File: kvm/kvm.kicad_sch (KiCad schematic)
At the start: 61 parts, among them J1 USB4110-GF-A, J2 USB4110-GF-A, J3 USB_A_Stacked, J4 USB_A_Stacked, Q1 Q_PMOS_GSD, SW1 SW_DPDT_x2, U1 SRV05-4, U2 LTC4412xS6, U3 FSUSB42MUX, U4 GL850G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

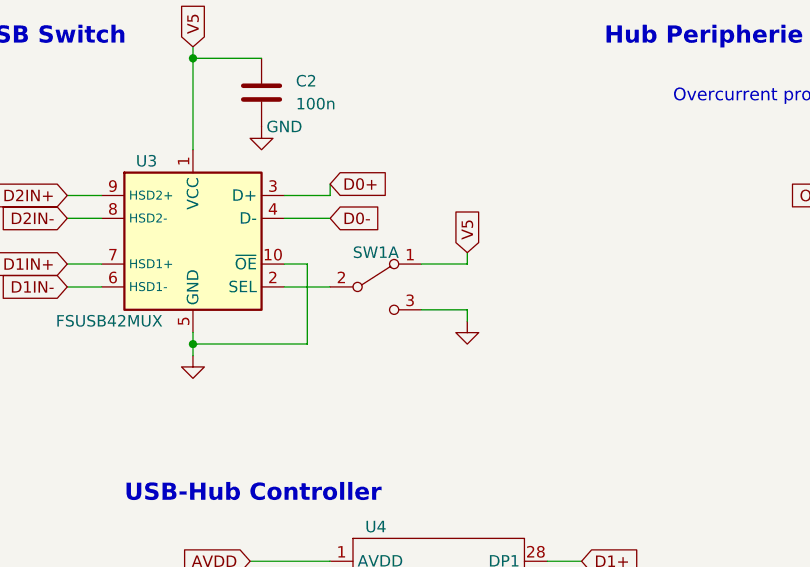
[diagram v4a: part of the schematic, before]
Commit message: fixed missing pull down on FSUSBMUX
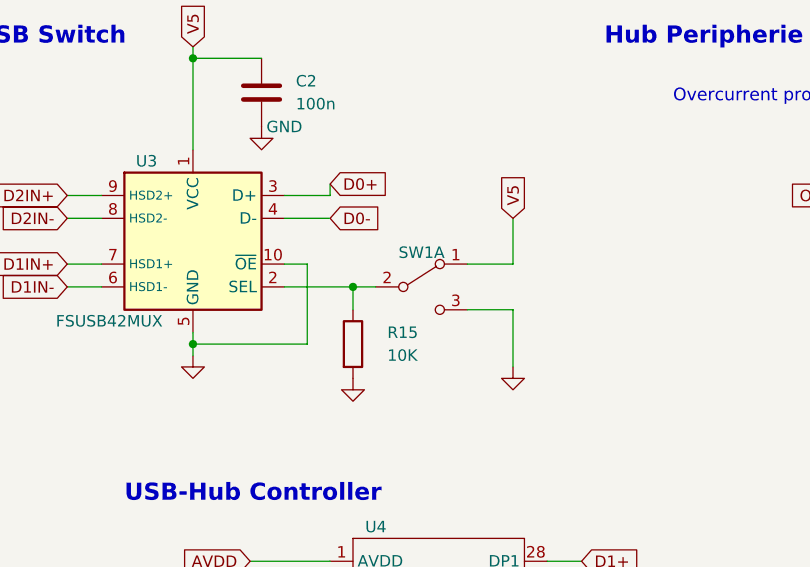
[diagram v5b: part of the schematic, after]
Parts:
- added R15: 10K, Resistor_SMD:R_0603_1608Metric_Pad0.98x0.95mm_HandSolder, symbol Device:R
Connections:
- net GND: now also R15.2
- net at SW1.2 (B), U3.2 (SEL): now also R15.1
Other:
- moved on the sheet: SW1A
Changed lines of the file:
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@@
   (junction (at 66.04 133.35) (diameter 0) (color 0 0 0 0)
   )
+  (junction (at 128.27 44.45) (diameter 0) (color 0 0 0 0)
+  )
   (junction (at 237.49 106.68) (diameter 0) (color 0 0 0 0)
   )
@@
     (stroke (width 0) (type default) (color 0 0 0 0))
   )
+  (wire (pts (xy 128.27 44.45) (xy 128.27 46.99))
+    (stroke (width 0) (type default) (color 0 0 0 0))
+  )
   (wire (pts (xy 273.05 124.46) (xy 270.51 124.46))
     (stroke (width 0) (type default) (color 0 0 0 0))
@@
     (stroke (width 0) (type default) (color 0 0 0 0))
   )
+  (wire (pts (xy 128.27 44.45) (xy 130.81 44.45))
+    (stroke (width 0) (type default) (color 0 0 0 0))
+  )
   (wire (pts (xy 29.21 158.75) (xy 33.02 158.75))
     (stroke (width 0) (type default) (color 0 0 0 0))
@@
     (stroke (width 0) (type default) (color 0 0 0 0))
   )
-  (wire (pts (xy 135.89 41.91) (xy 140.97 41.91))
+  (wire (pts (xy 140.97 41.91) (xy 146.05 41.91))
     (stroke (width 0) (type default) (color 0 0 0 0))
   )
@@
     (stroke (width 0) (type default) (color 0 0 0 0))
   )
-  (wire (pts (xy 135.89 46.99) (xy 140.97 46.99))
+  (wire (pts (xy 140.97 46.99) (xy 146.05 46.99))
     (stroke (width 0) (type default) (color 0 0 0 0))
   )
@@
     (stroke (width 0) (type default) (color 0 0 0 0))
   )
-  (wire (pts (xy 140.97 46.99) (xy 140.97 48.26))
+  (wire (pts (xy 146.05 46.99) (xy 146.05 53.34))
     (stroke (width 0) (type default) (color 0 0 0 0))
   )
@@
     (stroke (width 0) (type default) (color 0 0 0 0))
   )
-  (wire (pts (xy 140.97 40.64) (xy 140.97 41.91))
+  (wire (pts (xy 146.05 36.83) (xy 146.05 41.91))
     (stroke (width 0) (type default) (color 0 0 0 0))
   )
@@
     (stroke (width 0) (type default) (color 0 0 0 0))
   )
-  (wire (pts (xy 120.65 44.45) (xy 125.73 44.45))
+  (wire (pts (xy 120.65 44.45) (xy 128.27 44.45))
     (stroke (width 0) (type default) (color 0 0 0 0))
   )
@@
     )
   )
-  (global_label "V5" (shape input) (at 140.97 40.64 90) (fields_autoplaced)
+  (global_label "V5" (shape input) (at 146.05 36.83 90) (fields_autoplaced)
     (effects (font (size 1.27 1.27)) (justify left))
-    (property "Intersheet References" "${INTERSHEET_REFS}" (id 0) (at 140.8906 35.9288 90)
+    (property "Intersheet References" "${INTERSHEET_REFS}" (id 0) (at 145.9706 32.1188 90)
       (effects (font (size 1.27 1.27)) (justify left) hide)
     )
@@
     (pin "2")
   )
+  (symbol (lib_id "power:GND") (at 128.27 54.61 0) (unit 1)
+    (in_bom yes) (on_board yes) (fields_autoplaced)
+    (property "Reference" "#PWR04" (id 0) (at 128.27 60.96 0)
+      (effects (font (size 1.27 1.27)) hide)
+    )
+    (property "Value" "GND" (id 1) (at 128.27 59.69 0)
+      (effects (font (size 1.27 1.27)) hide)
+    )
+    (property "Footprint" "" (id 2) (at 128.27 54.61 0)
+      (effects (font (size 1.27 1.27)) hide)
+    )
+    (property "Datasheet" "" (id 3) (at 128.27 54.61 0)
+      (effects (font (size 1.27 1.27)) hide)
+    )
+    (pin "1")
+  )
   (symbol (lib_id "Connector:USB_A_Stacked") (at 270.51 106.68 0) (mirror y) (unit 1)
     (in_bom yes) (on_board yes) (fields_autoplaced)
@@
     (pin "2")
   )
-  (symbol (lib_id "Switch:SW_DPDT_x2") (at 130.81 44.45 0) (unit 1)
+  (symbol (lib_id "Switch:SW_DPDT_x2") (at 135.89 44.45 0) (unit 1)
     (in_bom yes) (on_board yes)
-    (property "Reference" "SW1" (id 0) (at 130.81 40.64 0))
-    (property "Value" "SW_DPDT_x2" (id 1) (at 130.81 39.37 0)
+    (property "Reference" "SW1" (id 0) (at 135.89 40.64 0))
+    (property "Value" "SW_DPDT_x2" (id 1) (at 135.89 39.37 0)
       (effects (font (size 1.27 1.27)) hide)
     )
-    (property "Footprint" "Connector_PinHeader_2.54mm:PinHeader_1x03_P2.54mm_Vertical" (id 2) (at 130.81 44.45 0)
+    (property "Footprint" "Connector_PinHeader_2.54mm:PinHeader_1x03_P2.54mm_Vertical" (id 2) (at 135.89 44.45 0)
       (effects (font (size 1.27 1.27)) hide)
     )
-    (property "Datasheet" "~" (id 3) (at 130.81 44.45 0)
+    (property "Datasheet" "~" (id 3) (at 135.89 44.45 0)
       (effects (font (size 1.27 1.27)) hide)
     )
-    (property "MouserLink" "https://www.mouser.at/ProductDetail/Chip-Quik/HDR100IMP40M-G-V-TH?qs=Wj%2FVkw3K%252BMBASWNGaQOKpg%3D%3D" (id 4) (at 130.81 44.45 0)
+    (property "MouserLink" "https://www.mouser.at/ProductDetail/Chip-Quik/HDR100IMP40M-G-V-TH?qs=Wj%2FVkw3K%252BMBASWNGaQOKpg%3D%3D" (id 4) (at 135.89 44.45 0)
       (effects (font (size 1.27 1.27)) hide)
     )
@@
     (pin "2")
   )
-  (symbol (lib_id "power:GND") (at 140.97 48.26 0) (unit 1)
+  (symbol (lib_id "power:GND") (at 146.05 53.34 0) (unit 1)
     (in_bom yes) (on_board yes) (fields_autoplaced)
-    (property "Reference" "#PWR012" (id 0) (at 140.97 54.61 0)
+    (property "Reference" "#PWR012" (id 0) (at 146.05 59.69 0)
       (effects (font (size 1.27 1.27)) hide)
     )
-    (property "Value" "GND" (id 1) (at 140.97 53.34 0)
+    (property "Value" "GND" (id 1) (at 146.05 58.42 0)
       (effects (font (size 1.27 1.27)) hide)
     )
-    (property "Footprint" "" (id 2) (at 140.97 48.26 0)
+    (property "Footprint" "" (id 2) (at 146.05 53.34 0)
       (effects (font (size 1.27 1.27)) hide)
     )
-    (property "Datasheet" "" (id 3) (at 140.97 48.26 0)
+    (property "Datasheet" "" (id 3) (at 146.05 53.34 0)
       (effects (font (size 1.27 1.27)) hide)
     )
@@
     (pin "1")
   )
+  (symbol (lib_id "Device:R") (at 128.27 50.8 0) (unit 1)
+    (in_bom yes) (on_board yes)
+    (property "Reference" "R15" (id 0) (at 132.08 49.53 0)
+      (effects (font (size 1.27 1.27)) (justify left))
+    )
+    (property "Value" "10K" (id 1) (at 132.08 52.07 0)
+      (effects (font (size 1.27 1.27)) (justify left))
+    )
+    (property "Footprint" "Resistor_SMD:R_0603_1608Metric_Pad0.98x0.95mm_HandSolder" (id 2) (at 126.492 50.8 90)
+      (effects (font (size 1.27 1.27)) hide)
+    )
+    (property "Datasheet" "~" (id 3) (at 128.27 50.8 0)
+      (effects (font (size 1.27 1.27)) hide)
+    )
+    (property "MouserLink" "https://www.mouser.at/ProductDetail/Panasonic/ERJ-3EKF1002V?qs=sGAEpiMZZMtG0KNrPCHnjWXb3yLuGJ273jbET5rTjY4%3D" (id 4) (at 128.27 50.8 0)
+      (effects (font (size 1.27 1.27)) hide)
+    )
+    (pin "1")
+    (pin "2")
+  )
   (symbol (lib_id "power:GND") (at 15.24 78.74 0) (unit 1)
     (in_bom yes) (on_board yes) (fields_autoplaced)
@@
       (reference "#PWR03") (unit 1) (value "GND") (footprint "")
     )
+    (path "/11dc7ca4-4cbc-47eb-9ac5-3bdc24ff3539"
+      (reference "#PWR04") (unit 1) (value "GND") (footprint "")
+    )
     (path "/e1975629-2667-40d8-981e-fa10a1ed674b"
       (reference "#PWR09") (unit 1) (value "GND") (footprint "")
@@
       (reference "R14") (unit 1) (value "47K") (footprint "Resistor_SMD:R_0603_1608Metric_Pad0.98x0.95mm_HandSolder")
     )
+    (path "/e99a9d60-2551-4726-a170-8af4df4dab91"
+      (reference "R15") (unit 1) (value "10K") (footprint "Resistor_SMD:R_0603_1608Metric_Pad0.98x0.95mm_HandSolder")
+    )
     (path "/9ad80869-bc67-4607-bc59-59cf4f597de8"
